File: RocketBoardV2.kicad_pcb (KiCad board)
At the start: 2 copper layers, 4 parts, among them U1 SC0914_13_, U2 MT29F2G01ABAGDWB-IT-G, U3 BMI270

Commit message: started routing
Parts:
- added J1: 10118194-0001LF, Components:AMPHENOL_10118194-0001LF, F.Cu at (146.0, 91.6)
- added Y1: ABM8-272-T3, Components:XTAL_ABM8-272-T3, F.Cu at (146.6, 80.5)
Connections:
- A1 pad 10: unconnected-(A1-VDD-Pad10) -> +1V8
- A1 pad 2: unconnected-(A1-SCL/SCLK-Pad2) -> /SPI0_SCK
- A1 pad 3: unconnected-(A1-GND-Pad3) -> GND
- A1 pad 4: unconnected-(A1-SDA/SDI-Pad4) -> /SPI0_TX
- A1 pad 6: unconnected-(A1-~{CS}-Pad6) -> /BARO_CS
- A1 pad 7: unconnected-(A1-INT/SDO-Pad7) -> /SPI0_RX
- A1 pad 8: unconnected-(A1-GND__1-Pad8) -> GND
- A1 pad 9: unconnected-(A1-GND__2-Pad9) -> GND
- U1 pad 19: unconnected-(U1-TESTEN-Pad19) -> GND
- U1 pad 2: unconnected-(U1-GPIO0-Pad2) -> /SPI0_RX
- U1 pad 23: unconnected-(U1-DVDD-Pad23) -> +1V1
- U1 pad 3: unconnected-(U1-GPIO1-Pad3) -> /GYRO_CS
- U1 pad 4: unconnected-(U1-GPIO2-Pad4) -> /SPI0_SCK
- U1 pad 45: unconnected-(U1-VREG_VOUT-Pad45) -> +1V1
- U1 pad 46: unconnected-(U1-USB_DM-Pad46) -> Net-(U1-USB_DM)
- U1 pad 47: unconnected-(U1-USB_DP-Pad47) -> Net-(U1-USB_DP)
- U1 pad 5: unconnected-(U1-GPIO3-Pad5) -> /SPI0_TX
- U1 pad 50: unconnected-(U1-DVDD__1-Pad50) -> +1V1
- U1 pad 51: unconnected-(U1-QSPI_SD3-Pad51) -> /QSPI_SD3
- U1 pad 52: unconnected-(U1-QSPI_SCLK-Pad52) -> /QSPI_SCLK
- U1 pad 53: unconnected-(U1-QSPI_SD0-Pad53) -> /QSPI_SD0
- U1 pad 54: unconnected-(U1-QSPI_SD2-Pad54) -> /QSPI_SD2
- U1 pad 55: unconnected-(U1-QSPI_SD1-Pad55) -> /QSPI_SD1
- U1 pad 56: unconnected-(U1-QSPI_SS_N-Pad56) -> /QSPI_SS
- U1 pad 57: unconnected-(U1-GND-Pad57) -> GND
- U1 pad 6: unconnected-(U1-GPIO4-Pad6) -> /BARO_CS
- U2 pad 1: unconnected-(U2-~{CS}-Pad1) -> /QSPI_SS
- U2 pad 2: unconnected-(U2-SO/IO1-Pad2) -> /QSPI_SD1
- U2 pad 3: unconnected-(U2-~{WP}/IO2-Pad3) -> /QSPI_SD2
- U2 pad 4: unconnected-(U2-VSS-Pad4) -> GND
- U2 pad 5: unconnected-(U2-SI/IO0-Pad5) -> /QSPI_SD0
- U2 pad 6: unconnected-(U2-SCK-Pad6) -> /QSPI_SCLK
- U2 pad 7: unconnected-(U2-~{HOLD}/IO3-Pad7) -> /QSPI_SD3
- U3 pad 1: unconnected-(U3-SDO-Pad1) -> /SPI0_RX
- U3 pad 12: unconnected-(U3-CSB-Pad12) -> /GYRO_CS
- U3 pad 13: unconnected-(U3-SCX-Pad13) -> /SPI0_SCK
- U3 pad 14: unconnected-(U3-SDX-Pad14) -> /SPI0_TX
- U3 pad 5: unconnected-(U3-VDDIO-Pad5) -> +1V8
- U3 pad 6: unconnected-(U3-GNDIO-Pad6) -> GND
- U3 pad 7: unconnected-(U3-GND-Pad7) -> GND
- U3 pad 8: unconnected-(U3-VDD-Pad8) -> +1V8

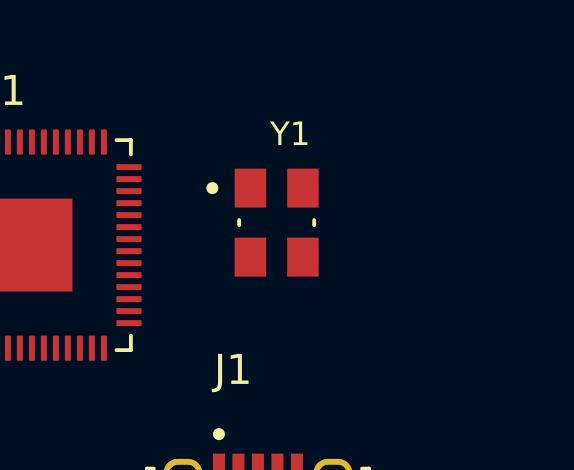
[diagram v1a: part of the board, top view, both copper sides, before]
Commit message: added PMIC
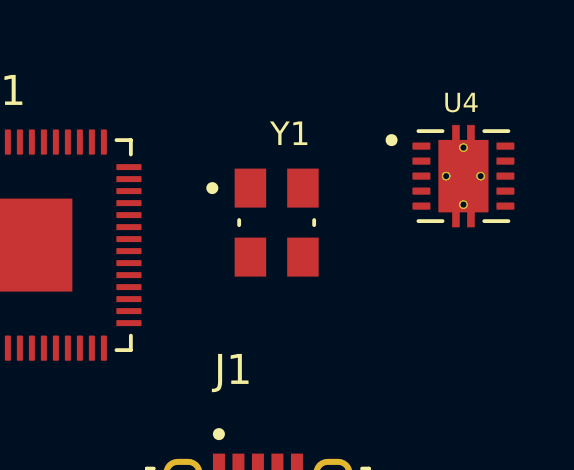
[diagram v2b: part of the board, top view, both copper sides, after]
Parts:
- added U4: TPS62420DRCR, Components:IC_TPS62420DRCR, F.Cu at (152.8, 79.0)
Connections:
- U1 pad 1: unconnected-(U1-IOVDD-Pad1) -> +3V3
- U1 pad 10: unconnected-(U1-IOVDD__1-Pad10) -> +3V3
- U1 pad 20: unconnected-(U1-XIN-Pad20) -> /XIN
- U1 pad 21: unconnected-(U1-XOUT-Pad21) -> /XOUT
- U1 pad 22: unconnected-(U1-IOVDD__2-Pad22) -> +3V3
- U1 pad 33: unconnected-(U1-IOVDD__3-Pad33) -> +3V3
- U1 pad 42: unconnected-(U1-IOVDD__4-Pad42) -> +3V3
- U1 pad 48: unconnected-(U1-USB_VDD-Pad48) -> +3V3
- U1 pad 49: unconnected-(U1-IOVDD__5-Pad49) -> +3V3
- Y1 pad 1: unconnected-(Y1-Pad1) -> /XIN
- Y1 pad 2: unconnected-(Y1-GND-Pad2) -> GND
- Y1 pad 3: unconnected-(Y1-Pad3) -> Net-(C8-Pad1)
- Y1 pad 4: unconnected-(Y1-GND__1-Pad4) -> GND

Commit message: some more power changes
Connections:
- U1 pad 24: unconnected-(U1-SWCLK-Pad24) -> Net-(U1-SWCLK)
- U1 pad 25: unconnected-(U1-SWDIO-Pad25) -> Net-(U1-SWDIO)
- U1 pad 37: unconnected-(U1-GPIO25-Pad37) -> /LED
- U2 pad 8: unconnected-(U2-VCC-Pad8) -> +3V3

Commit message: changed flash, power changes
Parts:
- added IC1: W25Q256JVEIQ, Components:SON127P800X600X80-9N, F.Cu at (137.7, 98.4)
- added J3: Conn_01x03_Pin, Connector_PinHeader_2.54mm:PinHeader_1x03_P2.54mm_Horizontal, F.Cu at (152.4, 97.7)
- added S1: TL3315NF250Q, Components:SW_TL3315NF250Q, F.Cu at (127.0, 96.6)
- added S2: TL3315NF250Q, Components:SW_TL3315NF250Q, F.Cu at (127.0, 102.8)
- added VR1: UA78L05ACPK, Components:VREG_UA78L05ACPK, F.Cu at (143.5, 106.2)
- U2: value MT29F2G01ABAGDWB-IT-G -> W25Q16JVUXIQ_TR; footprint easyeda2kicad:U-PDFN-8_L6.0-W8.0-P1.27-BL -> Components:IC_W25Q16JVUXIQ_TR
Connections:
- U1 pad 13: unconnected-(U1-GPIO10-Pad13) -> /SPI1_SCK
- U1 pad 14: unconnected-(U1-GPIO11-Pad14) -> /SPI1_TX
- U1 pad 15: unconnected-(U1-GPIO12-Pad15) -> /SPI1_RX
- U1 pad 16: unconnected-(U1-GPIO13-Pad16) -> /FLASH_CS
- U1 pad 26: unconnected-(U1-RUN-Pad26) -> /RUN
- U1 pad 43: unconnected-(U1-ADC_AVDD-Pad43) -> +3V3
- U1 pad 44: unconnected-(U1-VREG_VIN-Pad44) -> +3V3

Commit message: basic layout
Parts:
- added H1: MountingHole, MountingHole:MountingHole_3mm, F.Cu at (125.5, 69.0)
- added H2: MountingHole, MountingHole:MountingHole_3mm, F.Cu at (144.0, 69.0)
- added H3: MountingHole, MountingHole:MountingHole_3mm, F.Cu at (144.0, 102.5)
- added H4: MountingHole, MountingHole:MountingHole_3mm, F.Cu at (125.5, 102.5)
- added TP3: TestPoint, TestPoint:TestPoint_Pad_3.0x3.0mm, B.Cu at (126.2, 85.0)
- added TP4: TestPoint, TestPoint:TestPoint_Pad_3.0x3.0mm, B.Cu at (131.3, 85.0)
- J3: moved to B.Cu
- moved U4 28.0 mm to (129.3, 94.2)
- moved J1 26.3 mm to (136.0, 67.3), turned to 180 degrees
- moved IC1 19.5 mm to (127.6, 81.7), turned to 90 degrees
- moved U3 17.0 mm to (125.2, 74.6), turned to -90 degrees
- moved A1 16.5 mm to (129.5, 74.8), turned to 180 degrees
- moved J3 15.9 mm to (139.8, 88.0), turned to -90 degrees
- moved Y1 13.4 mm to (135.3, 87.9), turned to -90 degrees
- moved VR1 12.4 mm to (140.2, 94.2)
- moved S1 12.0 mm to (137.8, 102.0)
- moved U2 11.1 mm to (132.8, 74.2), turned to -90 degrees
- moved S2 4.81 mm to (131.8, 102.0)
- moved U1 1.05 mm to (139.2, 80.8)
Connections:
- net VBUS renamed Net-(D4-A)
- IC1 pad 3: +3V3 -> Net-(IC1-DO_(IO1)_2)
- IC1 pad 7: +3V3 -> Net-(IC1-IO3)
- J3 pad 1: unconnected-(J3-Pin_1-Pad1) -> /SERVO
- U1 pad 7: unconnected-(U1-GPIO5-Pad7) -> /SERVO
- VR1 pad 1: unconnected-(VR1-OUTPUT-Pad1) -> Net-(D3-A)
- VR1 pad 2: unconnected-(VR1-COMMON-Pad2) -> GND
- VR1 pad 3: unconnected-(VR1-INPUT-Pad3) -> +BATT
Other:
- board outline added: 25 x 40 mm

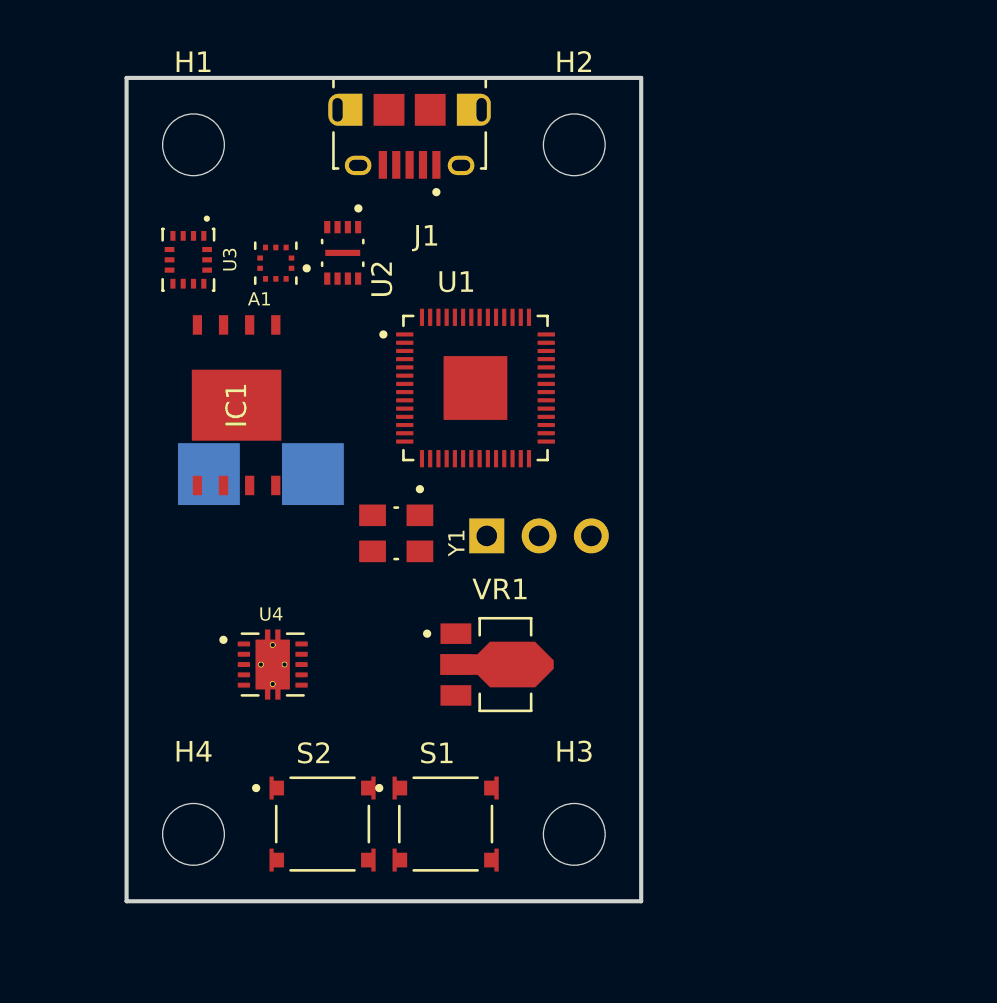
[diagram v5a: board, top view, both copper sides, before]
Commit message: more finalized layout, placed C + R
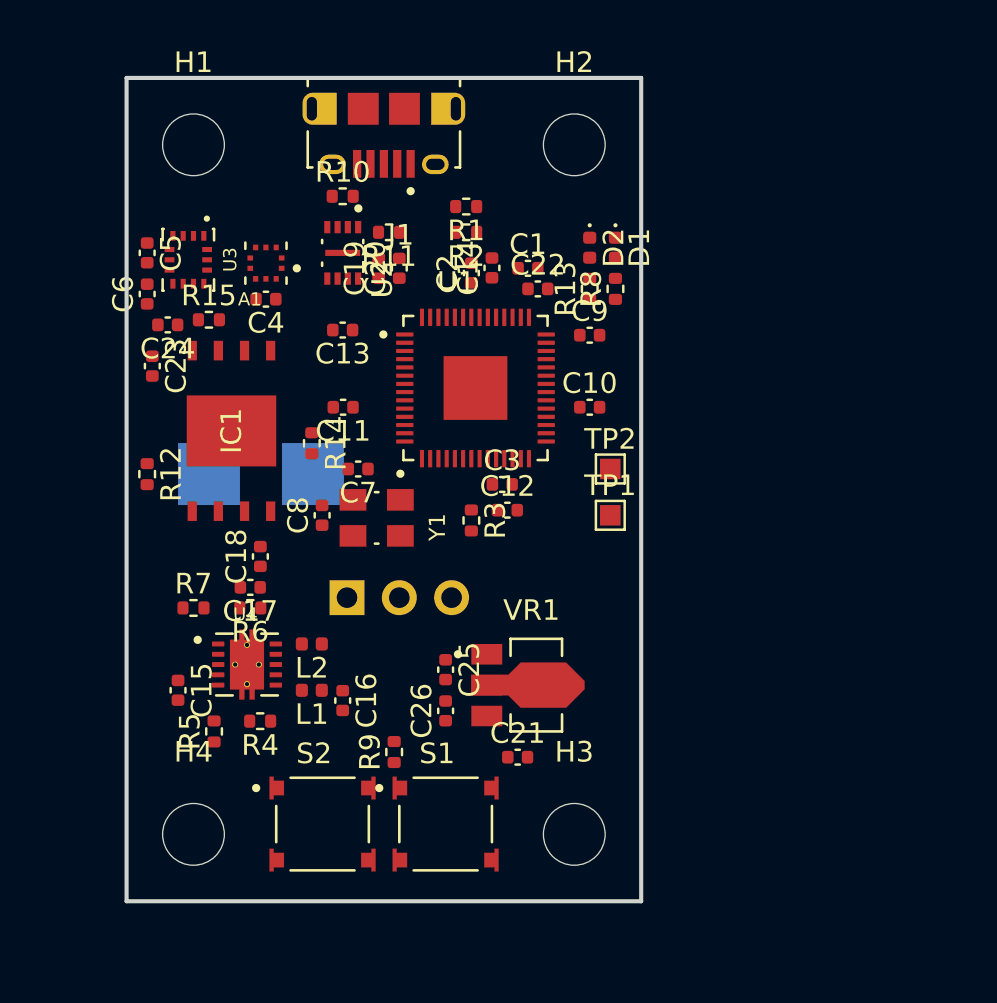
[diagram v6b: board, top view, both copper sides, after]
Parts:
- added C1: 1uF, Capacitor_SMD:C_0402_1005Metric, F.Cu at (141.8, 75.0)
- added C10: 0.1uF, Capacitor_SMD:C_0402_1005Metric, F.Cu at (144.8, 81.8)
- added C11: 0.1uF, Capacitor_SMD:C_0402_1005Metric, F.Cu at (132.8, 81.8)
- added C12: 0.1uF, Capacitor_SMD:C_0402_1005Metric, F.Cu at (140.8, 86.8)
- added C13: 0.1uF, Capacitor_SMD:C_0402_1005Metric, F.Cu at (132.8, 78.0)
- added C14: 0.1uF, Capacitor_SMD:C_0402_1005Metric, F.Cu at (140.0, 75.0)
- added C15: 10uF, Capacitor_SMD:C_0402_1005Metric, F.Cu at (124.8, 95.5)
- added C16: 22uF, Capacitor_SMD:C_0402_1005Metric, F.Cu at (132.8, 96.0)
- added C17: 33pF, Capacitor_SMD:C_0402_1005Metric, F.Cu at (128.3, 90.5)
- added C18: 22uF, Capacitor_SMD:C_0402_1005Metric, F.Cu at (128.8, 89.0)
- added C19: 0.1uF, Capacitor_SMD:C_0402_1005Metric, F.Cu at (134.5, 75.0)
- added C2: 1uF, Capacitor_SMD:C_0402_1005Metric, F.Cu at (139.0, 75.2)
- added C20: 2.2uF, Capacitor_SMD:C_0402_1005Metric, F.Cu at (135.5, 75.0)
- added C21: 1uF, Capacitor_SMD:C_0402_1005Metric, F.Cu at (141.2, 98.8)
- added C22: 1uF, Capacitor_SMD:C_0402_1005Metric, F.Cu at (142.2, 76.0)
- added C23: 2.2uF, Capacitor_SMD:C_0402_1005Metric, F.Cu at (123.5, 79.8)
- added C24: 0.1uF, Capacitor_SMD:C_0402_1005Metric, F.Cu at (124.2, 77.8)
- added C25: 0.1uF, Capacitor_SMD:C_0402_1005Metric, F.Cu at (137.8, 94.5)
- added C26: 0.33uF, Capacitor_SMD:C_0402_1005Metric, F.Cu at (137.8, 96.5)
- added C3: 1uF, Capacitor_SMD:C_0402_1005Metric, F.Cu at (140.5, 85.5)
- added C4: 0.1uF, Capacitor_SMD:C_0402_1005Metric, F.Cu at (129.0, 76.5)
- added C5: 0.1uF, Capacitor_SMD:C_0402_1005Metric, F.Cu at (123.2, 74.2)
- added C6: 0.1uF, Capacitor_SMD:C_0402_1005Metric, F.Cu at (123.2, 76.2)
- added C7: 15pF, Capacitor_SMD:C_0402_1005Metric, F.Cu at (133.5, 84.8)
- added C8: 15pF, Capacitor_SMD:C_0402_1005Metric, F.Cu at (131.8, 87.0)
- added C9: 0.1uF, Capacitor_SMD:C_0402_1005Metric, F.Cu at (144.8, 78.2)
- added D1: GREEN, LED_SMD:LED_0402_1005Metric, F.Cu at (146.0, 74.0)
- added D2: RED, LED_SMD:LED_0402_1005Metric, F.Cu at (144.8, 74.0)
- added L1: 2.2uH, Inductor_SMD:L_0402_1005Metric, F.Cu at (131.2, 95.5)
- added L2: 2.2uH, Inductor_SMD:L_0402_1005Metric, F.Cu at (131.2, 93.2)
- added R1: 27R, Resistor_SMD:R_0402_1005Metric, F.Cu at (138.8, 72.0)
- added R10: 1K, Resistor_SMD:R_0402_1005Metric, F.Cu at (132.8, 71.5)
- added R11: 10K, Resistor_SMD:R_0402_1005Metric, F.Cu at (135.0, 73.2)
- added R12: 10K, Resistor_SMD:R_0402_1005Metric, F.Cu at (123.2, 85.0)
- added R13: 470R, Resistor_SMD:R_0402_1005Metric, F.Cu at (144.8, 76.0)
- added R14: 10K, Resistor_SMD:R_0402_1005Metric, F.Cu at (131.2, 83.5)
- added R15: 10K, Resistor_SMD:R_0402_1005Metric, F.Cu at (126.2, 77.5)
- added R2: 27R, Resistor_SMD:R_0402_1005Metric, F.Cu at (138.8, 73.2)
- added R3: 1K, Resistor_SMD:R_0402_1005Metric, F.Cu at (139.0, 87.2)
- added R4: 810K, Resistor_SMD:R_0402_1005Metric, F.Cu at (128.7, 97.0)
- added R5: 180K, Resistor_SMD:R_0402_1005Metric, F.Cu at (126.5, 97.5)
- added R6: 360K, Resistor_SMD:R_0402_1005Metric, F.Cu at (128.3, 91.5)
- added R7: 180K, Resistor_SMD:R_0402_1005Metric, F.Cu at (125.5, 91.5)
- added R8: 470R, Resistor_SMD:R_0402_1005Metric, F.Cu at (146.0, 76.0)
- added R9: 470R, Resistor_SMD:R_0402_1005Metric, F.Cu at (135.2, 98.5)
- added TP1: TestPoint, TestPoint:TestPoint_Pad_1.0x1.0mm, F.Cu at (145.8, 87.0)
- added TP2: TestPoint, TestPoint:TestPoint_Pad_1.0x1.0mm, F.Cu at (145.8, 84.8)
- moved J3 7.42 mm to (133.0, 91.0)
- moved VR1 1.80 mm to (141.8, 95.2)
- moved IC1 1.27 mm to (127.3, 82.9)
- moved J1 1.25 mm to (134.8, 67.2)
- moved U4 1.25 mm to (128.1, 94.2)
- moved Y1 1.21 mm to (134.4, 87.1)
- moved A1 0.48 mm to (129.0, 74.8)
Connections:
- U4 pad 1: unconnected-(U4-ADJ2-Pad1) -> Net-(U4-ADJ2)
- U4 pad 10: unconnected-(U4-SW2-Pad10) -> Net-(U4-SW2)
- U4 pad 11: unconnected-(U4-EXP-Pad11) -> GND
- U4 pad 2: unconnected-(U4-MODE/DATA-Pad2) -> GND
- U4 pad 3: unconnected-(U4-VIN-Pad3) -> +5V
- U4 pad 4: unconnected-(U4-FB1-Pad4) -> +3V3
- U4 pad 5: unconnected-(U4-DEF_1-Pad5) -> Net-(U4-DEF_1)
- U4 pad 6: unconnected-(U4-SW1-Pad6) -> Net-(U4-SW1)
- U4 pad 7: unconnected-(U4-EN1-Pad7) -> +5V
- U4 pad 8: unconnected-(U4-GND-Pad8) -> GND
- U4 pad 9: unconnected-(U4-EN2-Pad9) -> +5V

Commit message: starting to route
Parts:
- removed S1, S2: TL3315NF250Q, Components:SW_TL3315NF250Q
- added D5: MSS1P4-M3_89A, Components:DIODE_MSS1P4-M3_89A, F.Cu at (144.0, 89.5)
- added D6: MSS1P4-M3_89A, Components:DIODE_MSS1P4-M3_89A, F.Cu at (140.8, 90.5)
- added LED1: WS2812B-MINI, easyeda2kicad:LED-SMD_4P-L3.5-W3.5-TL_WS2812B, B.Cu at (134.8, 79.1)
- added SW1: TS-1077S-02026, easyeda2kicad:SW-SMD_L3.1-W3.1-P2.20-LS4.0, F.Cu at (137.8, 102.0)
- added SW2: TS-1077S-02026, easyeda2kicad:SW-SMD_L3.1-W3.1-P2.20-LS4.0, F.Cu at (131.8, 102.0)
- C2: moved to B.Cu
- D1: value GREEN -> BLUE
- moved R14 9.65 mm to (126.2, 91.8), turned to 90 degrees
- moved C20 6.95 mm to (129.5, 71.5), turned to 180 degrees
- moved R12 6.13 mm to (124.5, 91.0), turned to 90 degrees
- moved R11 6.05 mm to (129.0, 72.5)
- moved R10 4.16 mm to (129.2, 73.8)
- moved C7 4.03 mm to (137.0, 86.8), turned to -90 degrees
- moved C2 3.31 mm to (138.5, 78.5), turned to 180 degrees
- moved C19 3.24 mm to (133.3, 72.0), turned to 180 degrees
- moved A1 2.75 mm to (129.0, 77.5), turned to 90 degrees
- moved R7 2.50 mm to (128.0, 91.5)
- moved IC1 2.41 mm to (126.4, 85.1)
- moved R15 2.36 mm to (125.0, 79.5), turned to -90 degrees
- moved C4 2.32 mm to (127.2, 78.0), turned to 90 degrees
- moved C18 2.30 mm to (131.0, 89.5), turned to 0 degrees
- moved C15 1.95 mm to (126.2, 94.2), turned to 180 degrees
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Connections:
- net Net-(U1-USB_DM) renamed /USB-
- net Net-(U1-USB_DP) renamed /USB+
- U1 pad 3: /GYRO_CS -> /BARO_CS
- U1 pad 36: unconnected-(U1-GPIO24-Pad36) -> /RGB_LED
- U1 pad 6: /BARO_CS -> /GYRO_CS
- U4 pad 12: (no net) -> GND
- U4 pad 13: (no net) -> GND
- U4 pad 14: (no net) -> GND
- U4 pad 15: (no net) -> GND
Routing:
- net +3V3: track 0.00 -> 52.8 mm
- net Net-(J1-VCC): track 0.00 -> 28.2 mm, vias 0 -> 2
- net /RUN: track 0.00 -> 25.7 mm, vias 0 -> 2
- net +5V: track 0.00 -> 18.3 mm
- net /FLASH_CS: track 0.00 -> 18.1 mm
- net /SPI0_SCK: track 0.00 -> 16.5 mm
- net /GYRO_CS: track 0.00 -> 14.9 mm
- net /SPI0_TX: track 0.00 -> 14.4 mm, vias 0 -> 3
- net /SPI1_RX: track 0.00 -> 13.6 mm
- net /SPI0_RX: track 0.00 -> 13.1 mm
- net /QSPI_SS: track 0.00 -> 12.9 mm
- net /SERVO: track 0.00 -> 11.9 mm, vias 0 -> 1
- net /QSPI_SD1: track 0.00 -> 10.6 mm
- net /SPI1_SCK: track 0.00 -> 10.2 mm
- net /QSPI_SD2: track 0.00 -> 9.78 mm
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
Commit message: initial routing done
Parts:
- moved TP1 0.50 mm to (145.2, 87.0)
- moved TP2 0.50 mm to (145.2, 84.8)
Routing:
- net +3V3: track 52.8 -> 122.4 mm
- net GND: track 7.68 -> 58.2 mm, vias 0 -> 25
- net Net-(R10-Pad1): track 0.00 -> 34.3 mm, vias 0 -> 2
- net +5V: track 18.3 -> 50.4 mm, vias 0 -> 1
- net +1V8: track 9.78 -> 35.1 mm, vias 0 -> 3
- net +1V1: track 8.36 -> 29.3 mm, vias 1 -> 3
- net +BATT: track 2.11 -> 19.7 mm, vias 0 -> 1
- net /RGB_LED: track 6.49 -> 9.38 mm
- net Net-(D2-A): track 0.00 -> 1.00 mm
- net Net-(D1-A): track 0.00 -> 1.00 mm
- net Net-(U1-SWDIO): track 6.52 -> 5.77 mm
- net Net-(J1-VCC): track 28.2 -> 27.6 mm
- net Net-(U1-SWCLK): track 7.25 -> 6.75 mm
- added copper zone on B.Cu, net GND
- added copper zone on F.Cu, net GND
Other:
- outline, holes or cut-outs redrawn
